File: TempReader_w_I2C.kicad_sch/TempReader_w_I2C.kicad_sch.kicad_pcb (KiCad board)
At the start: 4 copper layers, 40 x 41 mm, 41 parts, among them J1 NRF Pin Header, J2 BME Pin Header, U5 MIC5205-3.3YM5, Y1 16MH

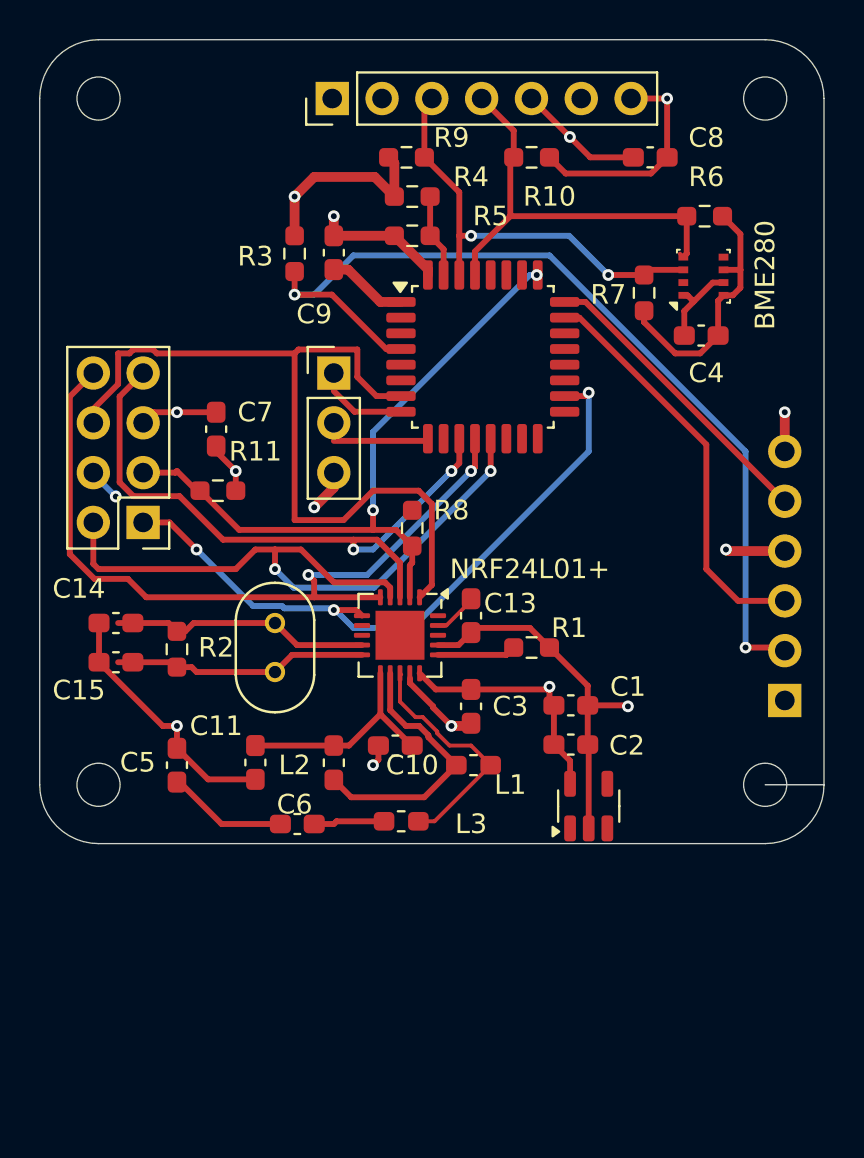
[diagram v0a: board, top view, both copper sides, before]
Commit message: Set payload length
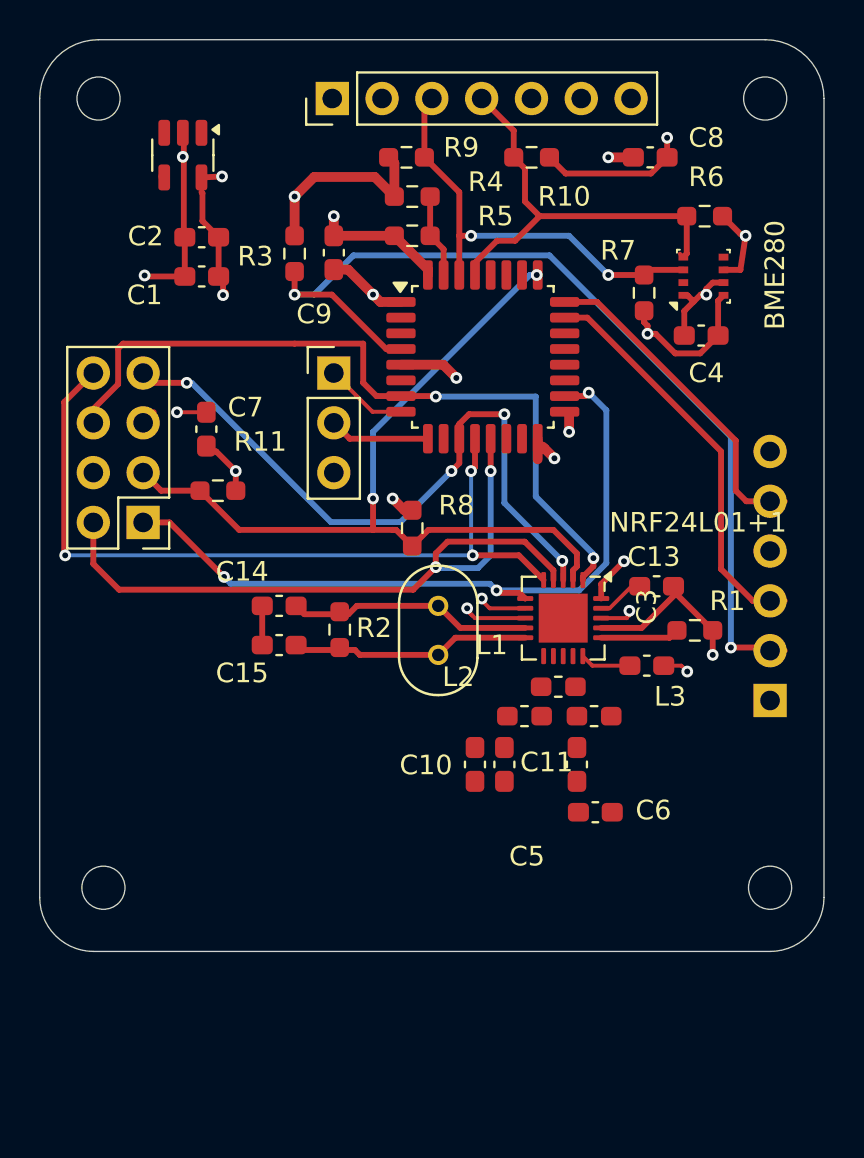
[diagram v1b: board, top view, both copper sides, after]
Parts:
- removed H2: MountingHole, MountingHole:MountingHole_2.2mm_M2
- added REF**: MountingHole_2.2mm_M2, MountingHole:MountingHole_2.2mm_M2, F.Cu at (158.0, 73.0)
- moved U5 39.1 mm to (162.3, 75.9), turned to -90 degrees
- moved C2 32.0 mm to (163.3, 80.1), turned to 180 degrees
- moved C1 28.9 mm to (163.3, 82.1), turned to 180 degrees
- moved C6 21.5 mm to (183.3, 109.4), turned to 0 degrees
- moved C5 14.6 mm to (182.4, 107.0), turned to -90 degrees
- moved C11 12.7 mm to (178.7, 107.0)
- moved L3 11.2 mm to (183.3, 104.5)
- moved L2 10.0 mm to (179.7, 104.5), turned to 180 degrees
- moved C13 9.58 mm to (186.5, 97.9), turned to 180 degrees
- moved C3 9.20 mm to (186.0, 101.9), turned to 180 degrees
- moved C14 8.37 mm to (167.2, 98.9)
- moved C15 8.37 mm to (167.2, 100.9)
- moved NRF24L01+1 8.37 mm to (181.7, 99.5)
- moved R1 8.37 mm to (188.4, 100.1)
- moved Y1 8.37 mm to (175.3, 100.1)
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- renumbered C6 to C5, C5 to C6, NRF24L01+ to NRF24L01+1
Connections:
- J2 pad 1: CS_BME -> unconnected-(J2-Pin_1-Pad1)
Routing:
- net GND1: track 65.0 -> 45.7 mm, vias 9 -> 11
- net Net-(NRF24L01+1-ANT1): track 13.8 -> 0.00 mm
- net Net-(NRF24L01+1-ANT2): track 12.4 -> 0.00 mm
- net Net-(NRF24L01+1-VDD_PA): track 11.4 -> 0.00 mm
- net CS_NRF: track 34.6 -> 42.7 mm
- net 50 O out: track 6.22 -> 0.00 mm
- net Net-(C5-Pad1): track 3.62 -> 0.00 mm
- net SPI_SCK: track 32.8 -> 36.1 mm, vias 2 -> 4
- net NRF_CE: track 42.0 -> 38.8 mm, vias 0 -> 2
- net NRF_IRQ: track 34.6 -> 37.6 mm
- net SPI_MOSI: track 35.6 -> 37.7 mm
- net +3V3: track 58.6 -> 57.1 mm, vias 6 -> 13
- net SW_CLK: track 15.4 -> 16.9 mm
- net SPI_MISO: track 40.0 -> 41.0 mm, vias 2 -> 3
- net Net-(NRF24L01+1-XC2): track 13.3 -> 12.5 mm
- added copper zone on In2.Cu, net +3V3
- added copper zone on In1.Cu, net GND1
- removed copper zone on In1.Cu, net +3V3
- removed copper zone on In2.Cu, net GND1
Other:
- board size 40 x 41 mm -> 40 x 46.5 mm

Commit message: Add ACK functionality
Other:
- board size 40 x 46.5 mm -> 40 x 55 mm
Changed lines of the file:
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@@
 			(outputformat 1)
 			(mirror no)
-			(drillshape 1)
+			(drillshape 0)
 			(scaleselection 1)
-			(outputdirectory "")
+			(outputdirectory "antenna_test_grb")
 		)
 	)
@@
 		)
 		(property "Value" "2.7nH"
-			(at 0 1.43 360)
+			(at 0 1.43 0)
 			(layer "F.Fab")
 			(effects
@@
 		)
 		(fp_text user "${REFERENCE}"
-			(at 0 0 360)
+			(at 0 0 0)
 			(layer "F.Fab")
 			(effects
@@
 		(tags "capacitor handsolder")
 		(property "Reference" "C1"
-			(at 2.9125 -0.95 360)
+			(at 2.9125 -0.95 0)
 			(layer "F.SilkS")
 			(effects
@@
 		)
 		(property "Value" "1uF"
-			(at 0 1.43 360)
+			(at 0 1.43 0)
 			(layer "F.Fab")
 			(effects
@@
 		)
 		(fp_text user "${REFERENCE}"
-			(at 0 0 360)
+			(at 0 0 0)
 			(layer "F.Fab")
 			(effects
@@
 		)
 		(property "Value" "1uF"
-			(at 0 1.43 360)
+			(at 0 1.43 0)
 			(layer "F.Fab")
 			(effects
@@
 		)
 		(fp_text user "${REFERENCE}"
-			(at 0 0 360)
+			(at 0 0 0)
 			(layer "F.Fab")
 			(effects
@@
 		)
 		(property "Value" "33nF"
-			(at 0 1.43 360)
+			(at 0 1.43 0)
 			(layer "F.Fab")
 			(effects
@@
 		)
 		(fp_text user "${REFERENCE}"
-			(at 0 0 360)
+			(at 0 0 0)
 			(layer "F.Fab")
 			(effects
@@
 		(tags "capacitor handsolder")
 		(property "Reference" "C2"
-			(at 2.8625 0.05 360)
+			(at 2.8625 0.05 0)
 			(layer "F.SilkS")
 			(effects
@@
 		)
 		(property "Value" "10uF"
-			(at 0 1.43 360)
+			(at 0 1.43 0)
 			(layer "F.Fab")
 			(effects
@@
 		)
 		(fp_text user "${REFERENCE}"
-			(at 0 0 360)
+			(at 0 0 0)
 			(layer "F.Fab")
 			(effects
@@
 		)
 		(property "Value" "1pF"
-			(at 0 1.43 360)
+			(at 0 1.43 0)
 			(layer "F.Fab")
 			(effects
@@
 		)
 		(fp_text user "${REFERENCE}"
-			(at 0 0 360)
+			(at 0 0 0)
 			(layer "F.Fab")
 			(effects
@@
 		(tags "SOT TO_SOT_SMD")
 		(property "Reference" "U5"
-			(at 0 -2.95 360)
+			(at 0 -2.95 0)
 			(layer "F.SilkS")
 			(hide yes)
@@
 	)
 	(gr_line
-		(start 195 113.75)
+		(start 195 122)
 		(end 195 73)
 		(stroke
@@
 	)
 	(gr_arc
-		(start 157.75 116.5)
-		(mid 155.805456 115.694544)
-		(end 155 113.75)
+		(start 158 125)
+		(mid 155.87868 124.12132)
+		(end 155 122)
+		(locked yes)
 		(stroke
 			(width 0.05)
@@
 		(mid 155.87868 70.87868)
 		(end 158 70)
+		(locked yes)
 		(stroke
 			(width 0.05)
@@
 	)
 	(gr_line
-		(start 157.75 116.5)
-		(end 192.25 116.5)
+		(start 158 125)
+		(end 192 125)
 		(stroke
 			(width 0.05)
@@
 		(mid 194.12132 70.87868)
 		(end 195 73)
+		(locked yes)
 		(stroke
 			(width 0.05)
@@
 	)
 	(gr_arc
-		(start 195 113.75)
-		(mid 194.194544 115.694544)
-		(end 192.25 116.5)
+		(start 195 122)
+		(mid 194.12132 124.12132)
+		(end 192 125)
+		(locked yes)
 		(stroke
 			(width 0.05)
@@
 	(gr_line
 		(start 155 73)
-		(end 155 113.75)
+		(end 155 122)
 		(stroke
 			(width 0.05)
